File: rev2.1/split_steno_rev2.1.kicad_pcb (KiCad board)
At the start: 2 copper layers, 99.7 x 74.8 mm, 67 parts, among them J1 USB_OTG, J2 Audio-Jack-4, P1 TC2030-IDC, SW1 SW_Push, SW10 SW_Push, SW11 SW_Push, SW12 SW_Push, SW13 SW_Push, SW14 SW_Push, SW15 SW_Push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

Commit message: reorganized pins, removed NO USB jumper
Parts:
- removed JP3: Jumper, jumper:Jumper_1x02_P2.54mm_THT
- JP1: value Jumper -> BATT CHECK
- JP2: value Jumper -> NO SW
- P1: footprint Tag-Connect:TC2030-NL_SMALL_AND_IDC_PDI_Extra_Pads -> Tag-Connect:TC2030-NL_SMALL_AND_IDC_PDI
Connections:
- U5 pad 1: /KEY16 -> /KEY9
- U5 pad 10: /UNDER_LED -> Net-(U5-Pad10)
- U5 pad 11: /VBUS_CHECK -> /UNDER_LED
- U5 pad 12: Net-(U5-Pad12) -> /CE
- U5 pad 13: Net-(U5-Pad13) -> /IRQ
- U5 pad 2: /KEY17 -> /KEY10
- U5 pad 20: /KEY5 -> /KEY11
- U5 pad 21: /KEY6 -> /KEY12
- U5 pad 23: /KEY13 -> /KEY6
- U5 pad 24: /KEY9 -> /KEY1
- U5 pad 25: /KEY10 -> /KEY2
- U5 pad 3: /KEY18 -> /KEY5
- U5 pad 32: /KEY3 -> /BAT_LVL
- U5 pad 33: /KEY4 -> /VBUS_CHECK
- U5 pad 36: /KEY1 -> /KEY15
- U5 pad 37: /KEY2 -> /KEY14
- U5 pad 4: Net-(U5-Pad4) -> /KEY4
- U5 pad 40: /KEY11 -> /KEY13
- U5 pad 41: /KEY12 -> /KEY8
- U5 pad 42: /KEY8 -> /KEY16
- U5 pad 43: /KEY14 -> /KEY17
- U5 pad 44: /KEY15 -> /KEY18
- U5 pad 5: /BAT_LVL -> /KEY3
- U5 pad 6: /CE -> Net-(U5-Pad6)
- U5 pad 7: /IRQ -> Net-(U5-Pad7)

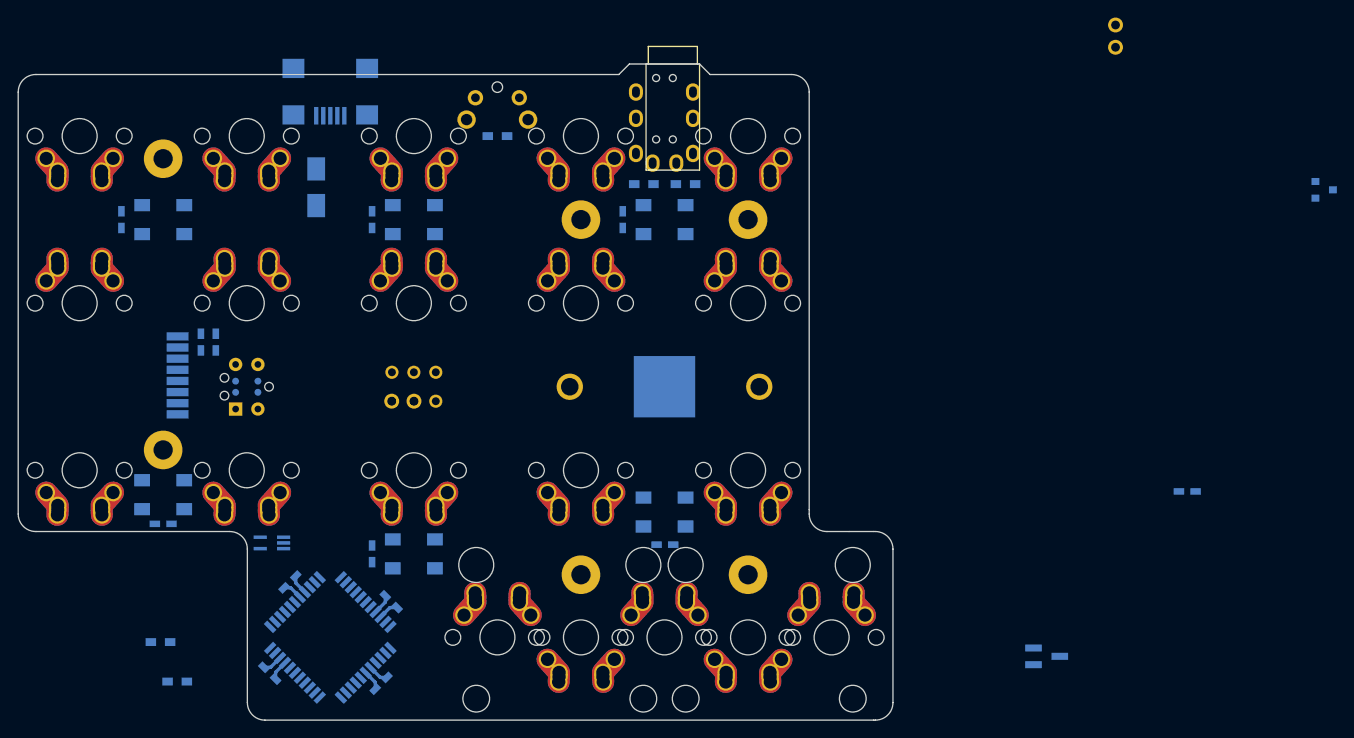
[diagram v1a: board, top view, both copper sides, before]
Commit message: laid out components
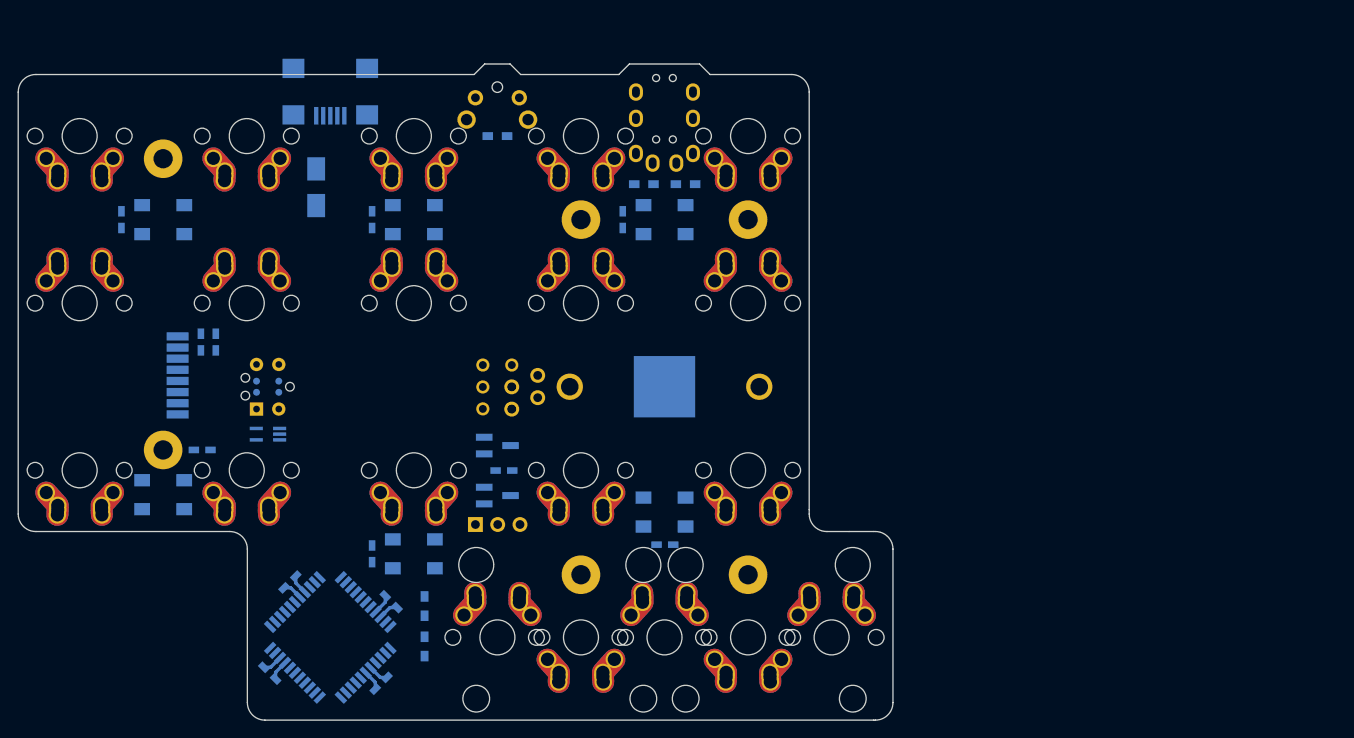
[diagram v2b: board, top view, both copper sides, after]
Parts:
- added J3: Conn_01x03, Pin_Headers:Pin_Header_Straight_1x03_Pitch2.54mm, B.Cu at (85.6, 118.1)
- JP1: value BATT CHECK -> BAT CHK
- SW14, SW3, SW4, SW7: footprint Keebio-Parts:Hybrid_PCB_100H_Dual_hole -> Keebio-Parts:Hybrid_PCB_100H_Dual_hole-flip
- U4: footprint TO_SOT_Packages_SMD:SOT-23 -> TO_SOT_Packages_SMD:SOT-23_Handsoldering
- moved U4 100.5 mm to (88.1, 114.8)
- moved C8 77.9 mm to (88.8, 112.0)
- moved JP1 75.8 mm to (92.7, 101.1), turned to 180 degrees
- moved D1 67.1 mm to (88.1, 109.1)
- moved R5 30.4 mm to (79.8, 127.4), turned to 90 degrees
- moved R4 28.5 mm to (79.8, 132.0), turned to 90 degrees
- moved U1 12.4 mm to (62.0, 107.8)
- moved JP2 11.3 mm to (89.7, 102.4), turned to 180 degrees
- moved C1 9.53 mm to (54.5, 109.6), turned to 180 degrees
- moved PWR 9.51 mm to (88.1, 102.4), turned to 90 degrees
- moved PDI 2.38 mm to (61.9, 102.4)
- renumbered U5 to ATXMEGA, BT1 to CR2032, P1 to PDI, SW22 to PWR, SW21 to RST, U6 to nRF24L01
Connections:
- ATXMEGA pad 20: /KEY11 -> /KEY12
- ATXMEGA pad 21: /KEY12 -> /KEY11
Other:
- outline, holes or cut-outs redrawn

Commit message: routed USB, left side switches
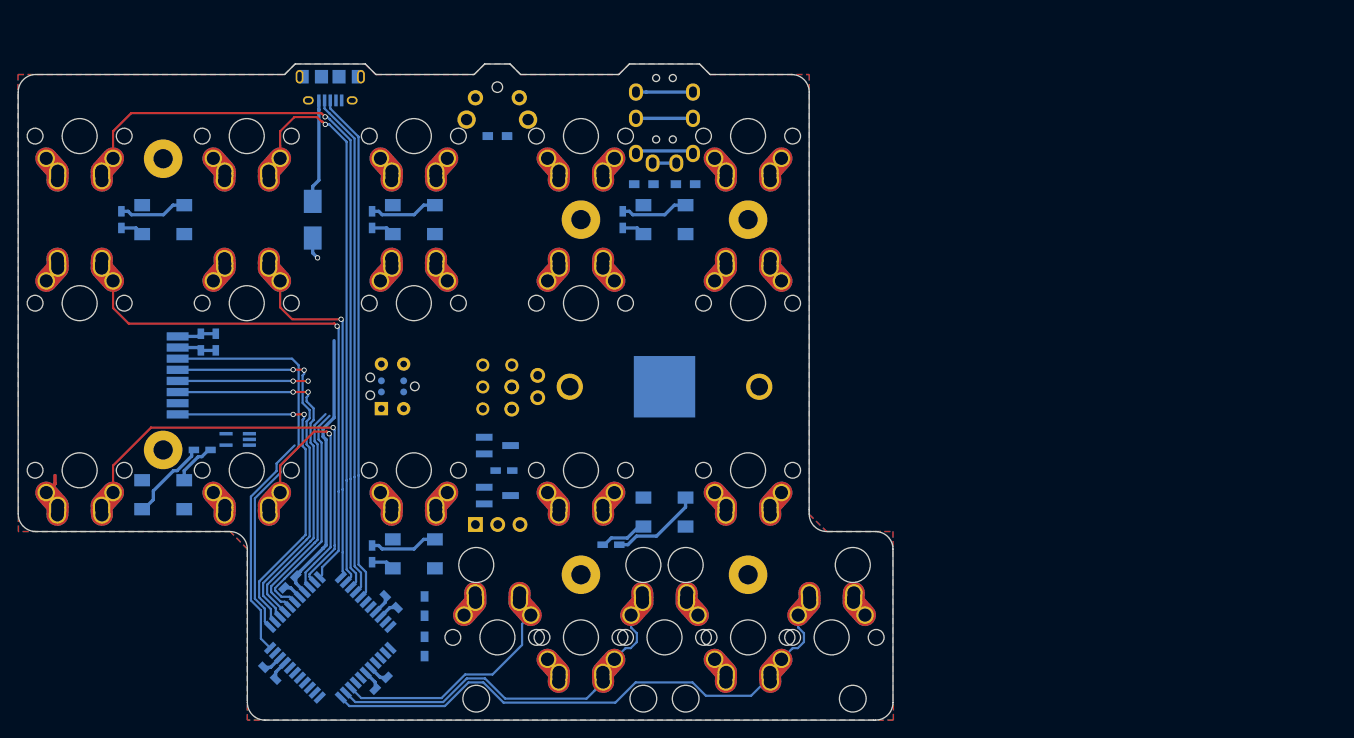
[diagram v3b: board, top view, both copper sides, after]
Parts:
- removed J1: USB_OTG, keyboard_parts:USB_miniB
- added USB: USB_OTG, conn_usb:USB_MicroB_Amphenol_10118194-0001LF, B.Cu at (69.0, 67.0)
- moved PDI 14.2 mm to (76.2, 102.3)
- moved C5 6.15 mm to (101.0, 120.4)
- moved F1 3.72 mm to (67.0, 83.3)
- moved U1 3.50 mm to (58.5, 108.4)
- turned C1 to 0 degrees
- renumbered CR2032 to BT1, ATXMEGA to U5, nRF24L01 to U6
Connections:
- U5 pad 22: /KEY7 -> /KEY6
- U5 pad 23: /KEY6 -> /KEY7
- U5 pad 24: /KEY1 -> /KEY2
- U5 pad 25: /KEY2 -> /KEY1
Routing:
- net /KEY1: track 0.00 -> 83.8 mm, vias 0 -> 1
- net /KEY2: track 0.00 -> 63.2 mm, vias 0 -> 1
- net /KEY18: track 0.00 -> 60.6 mm
- net /KEY6: track 0.00 -> 59.3 mm, vias 0 -> 1
- net /D+: track 0.00 -> 58.6 mm
- net /D-: track 0.00 -> 58.0 mm
- net +5V: track 0.00 -> 54.4 mm, vias 0 -> 1
- net /KEY11: track 0.00 -> 49.1 mm, vias 0 -> 1
- net /CE: track 0.00 -> 47.2 mm
- net /CSN: track 0.00 -> 46.7 mm, vias 0 -> 2
- net /MOSI: track 0.00 -> 44.1 mm, vias 0 -> 2
- net /IRQ: track 0.00 -> 41.7 mm, vias 0 -> 2
- net /SCK: track 0.00 -> 40.9 mm, vias 0 -> 2
- net /KEY7: track 0.00 -> 39.7 mm, vias 0 -> 1
- net /KEY17: track 0.00 -> 39.4 mm
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- added copper zone on B.Cu, net GND
- added copper zone on F.Cu, net GND
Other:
- outline, holes or cut-outs redrawn

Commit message: nrf and usb on both sides of board, rerouted
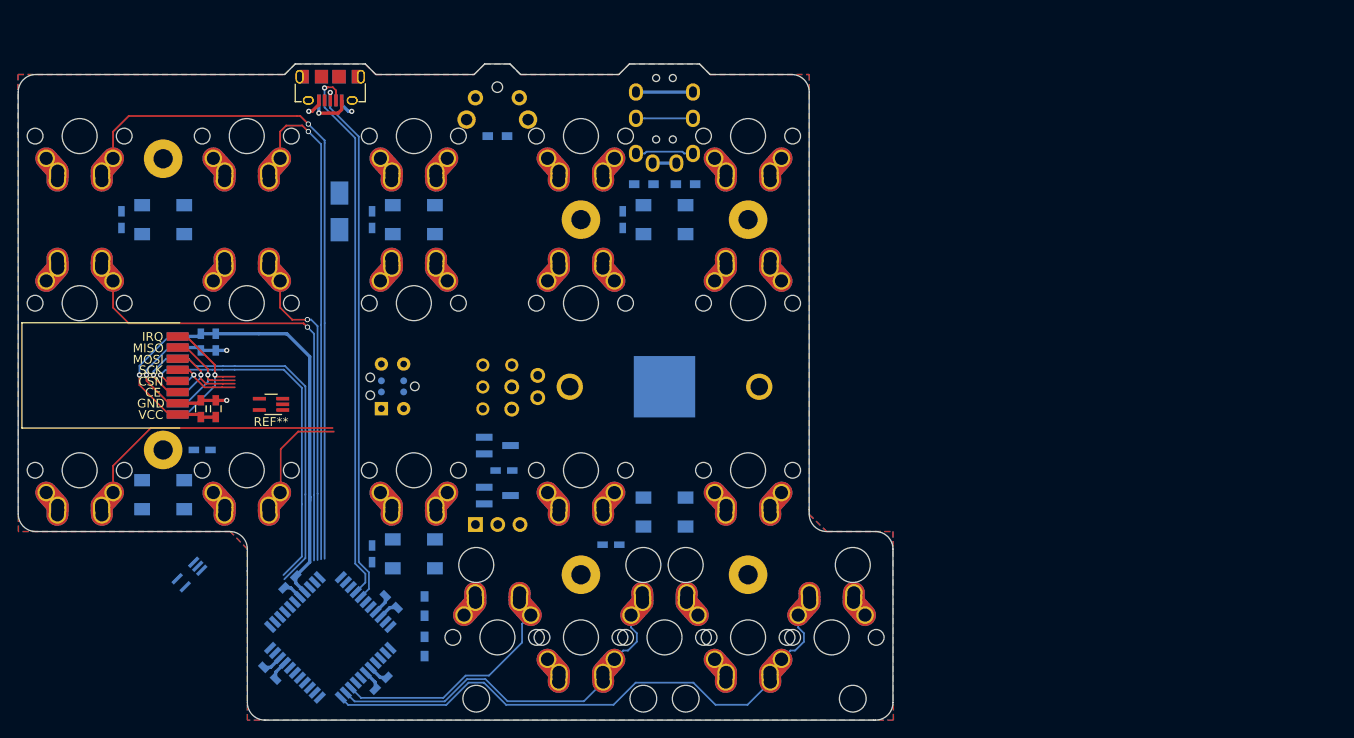
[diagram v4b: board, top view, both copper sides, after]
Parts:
- added REF**: nRF24L01_module, nordic:NRF24L01-Module-SMD, F.Cu at (50.9, 101.1)
- added REF**: C_0603_HandSoldering, Capacitors_SMD:C_0603_HandSoldering, F.Cu at (56.0, 104.9)
- added REF**: C_0603_HandSoldering, Capacitors_SMD:C_0603_HandSoldering, F.Cu at (54.3, 104.9)
- added REF**: USB_MicroB_Amphenol_10118194-0001LF, conn_usb:USB_MicroB_Amphenol_10118194-0001LF, F.Cu at (69.0, 67.0)
- added REF**: SOT-353_SC-70-5_Handsoldering, TO_SOT_Packages_SMD:SOT-353_SC-70-5_Handsoldering, F.Cu at (62.3, 104.4)
- USB: value USB_OTG -> J1
- moved U1 16.4 mm to (53.0, 123.8), turned to 225 degrees
- moved F1 3.19 mm to (70.1, 82.4)
- renumbered PDI to P1
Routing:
- net +5V: track 54.4 -> 0.00 mm, vias 1 -> 0
- net /SCK: track 40.9 -> 10.5 mm, vias 2 -> 1
- net /MOSI: track 44.1 -> 13.8 mm, vias 2 -> 1
- net VCC: track 43.1 -> 69.7 mm, vias 0 -> 1
- net /UNDER_LED: track 26.1 -> 0.00 mm
- net /IRQ: track 41.7 -> 17.1 mm, vias 2 -> 1
- net /KEY11: track 49.1 -> 29.8 mm, vias 1 -> 0
- net /KEY12: track 29.4 -> 11.9 mm, vias 1 -> 0
- net /MISO: track 26.0 -> 14.8 mm, vias 0 -> 1
- net /KEY1: track 83.8 -> 76.8 mm
- net /KEY2: track 63.2 -> 56.2 mm
- net Net-(F1-Pad1): track 11.8 -> 5.27 mm, vias 0 -> 1
- net /KEY6: track 59.3 -> 53.0 mm
- net /CSN: track 46.7 -> 41.2 mm, vias 2 -> 1
- net GND: track 46.5 -> 41.5 mm, vias 0 -> 5
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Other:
- rule trace_min: 0.2 -> 0.1524

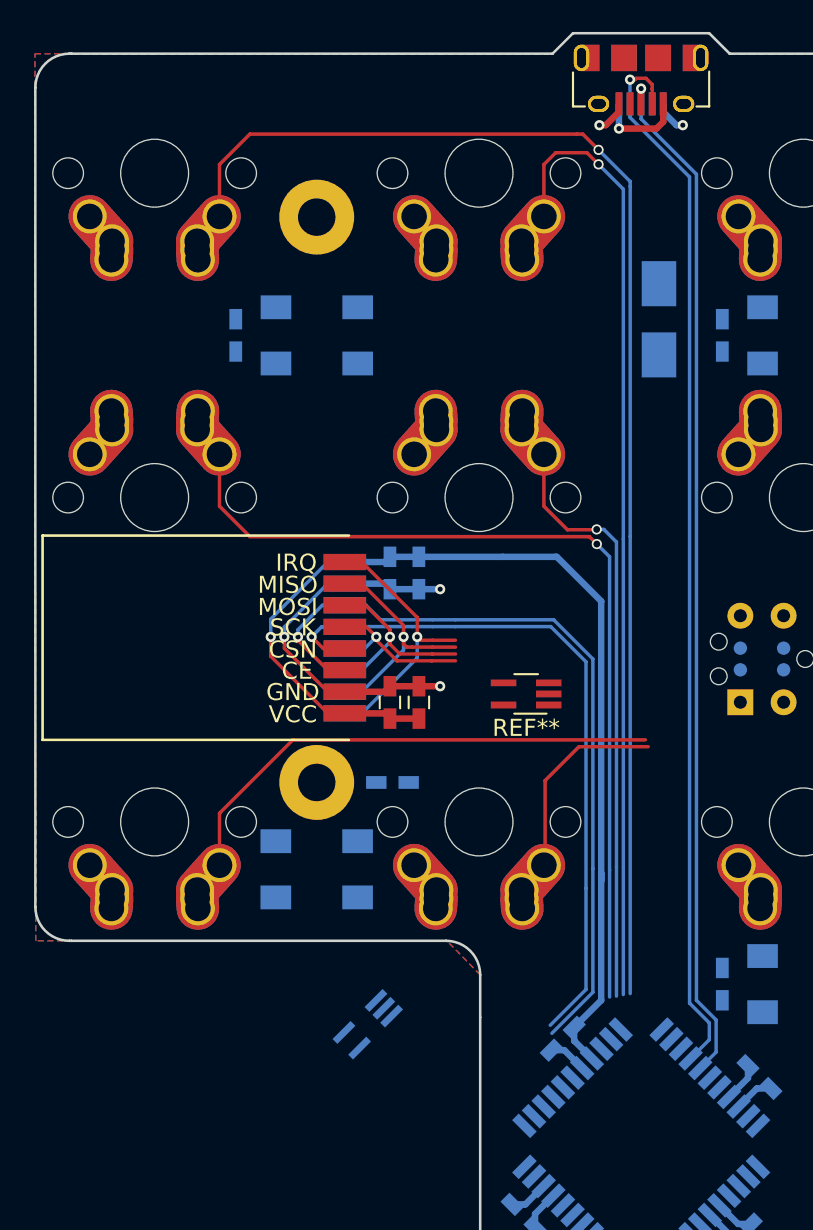
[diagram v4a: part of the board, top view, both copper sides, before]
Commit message: rerouted left half
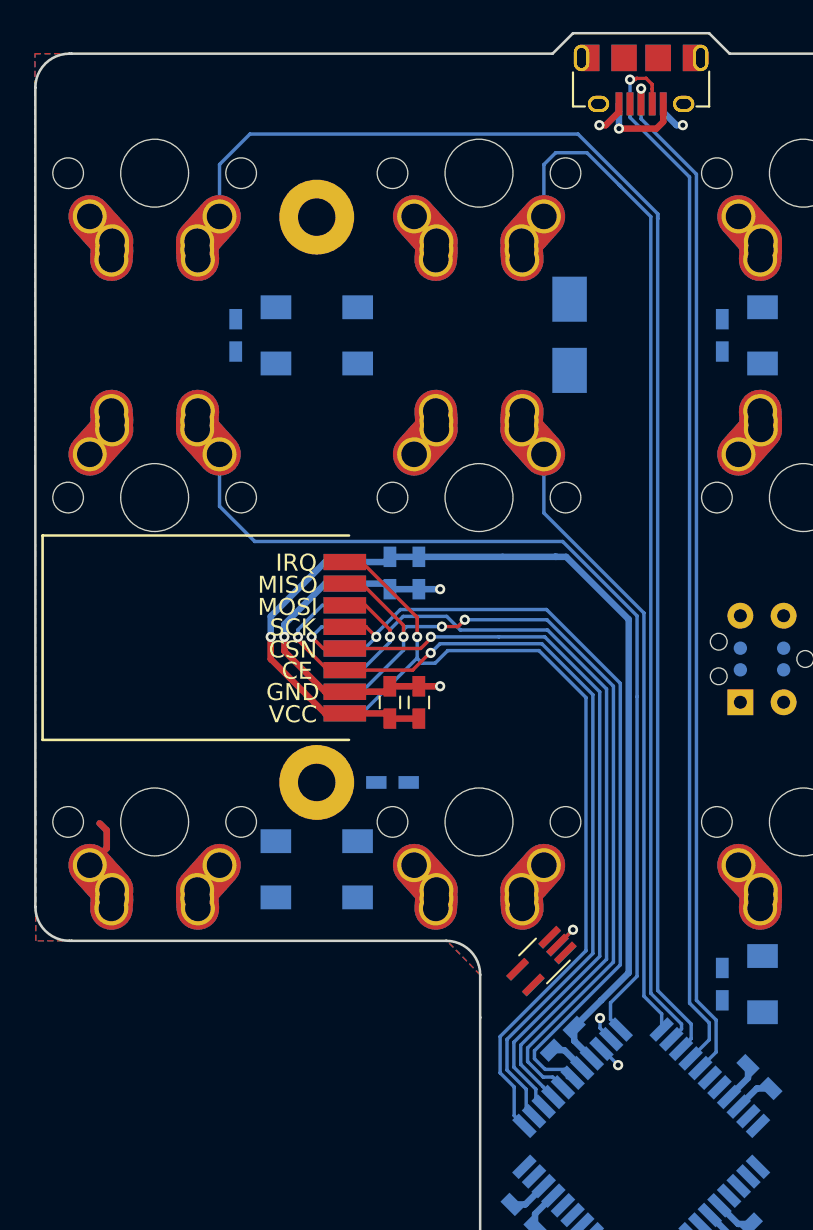
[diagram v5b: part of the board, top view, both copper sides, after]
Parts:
- moved REF** 15.7 mm to (63.2, 120.1), turned to 225 degrees
- moved U1 10.9 mm to (63.2, 120.1)
- moved F1 5.33 mm to (64.8, 83.3)
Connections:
- REF** pad 2: (no net) -> /UNDER_LED
- REF** pad 3: (no net) -> GND
- REF** pad 4: (no net) -> Net-(LED1-Pad4)
- REF** pad 5: (no net) -> +5V
- U5 pad 12: /CE -> /IRQ
- U5 pad 13: /IRQ -> /CE
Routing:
- net /SCK: track 10.5 -> 49.2 mm
- net /MISO: track 14.8 -> 52.8 mm, vias 1 -> 3
- net /MOSI: track 13.8 -> 51.4 mm
- net /IRQ: track 17.1 -> 53.9 mm
- net /KEY11: track 29.8 -> 1.51 mm, vias 0 -> 1
- net /KEY12: track 11.9 -> 1.47 mm, vias 0 -> 1
- net GND: track 41.5 -> 48.9 mm
- net /CSN: track 41.2 -> 47.8 mm, vias 1 -> 2
- net /KEY1: track 76.8 -> 81.9 mm, vias 1 -> 0
- net /CE: track 48.9 -> 54.0 mm, vias 1 -> 2
- net /KEY2: track 56.2 -> 60.6 mm, vias 1 -> 0
- net VCC: track 69.7 -> 72.3 mm
- net /UNDER_LED: track 0.00 -> 2.56 mm, vias 0 -> 1
- net /KEY6: track 53.0 -> 55.4 mm, vias 1 -> 0
- net /KEY7: track 34.9 -> 36.6 mm, vias 1 -> 0
